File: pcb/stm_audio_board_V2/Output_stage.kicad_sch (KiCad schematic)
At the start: 29 parts, among them U2 OP275

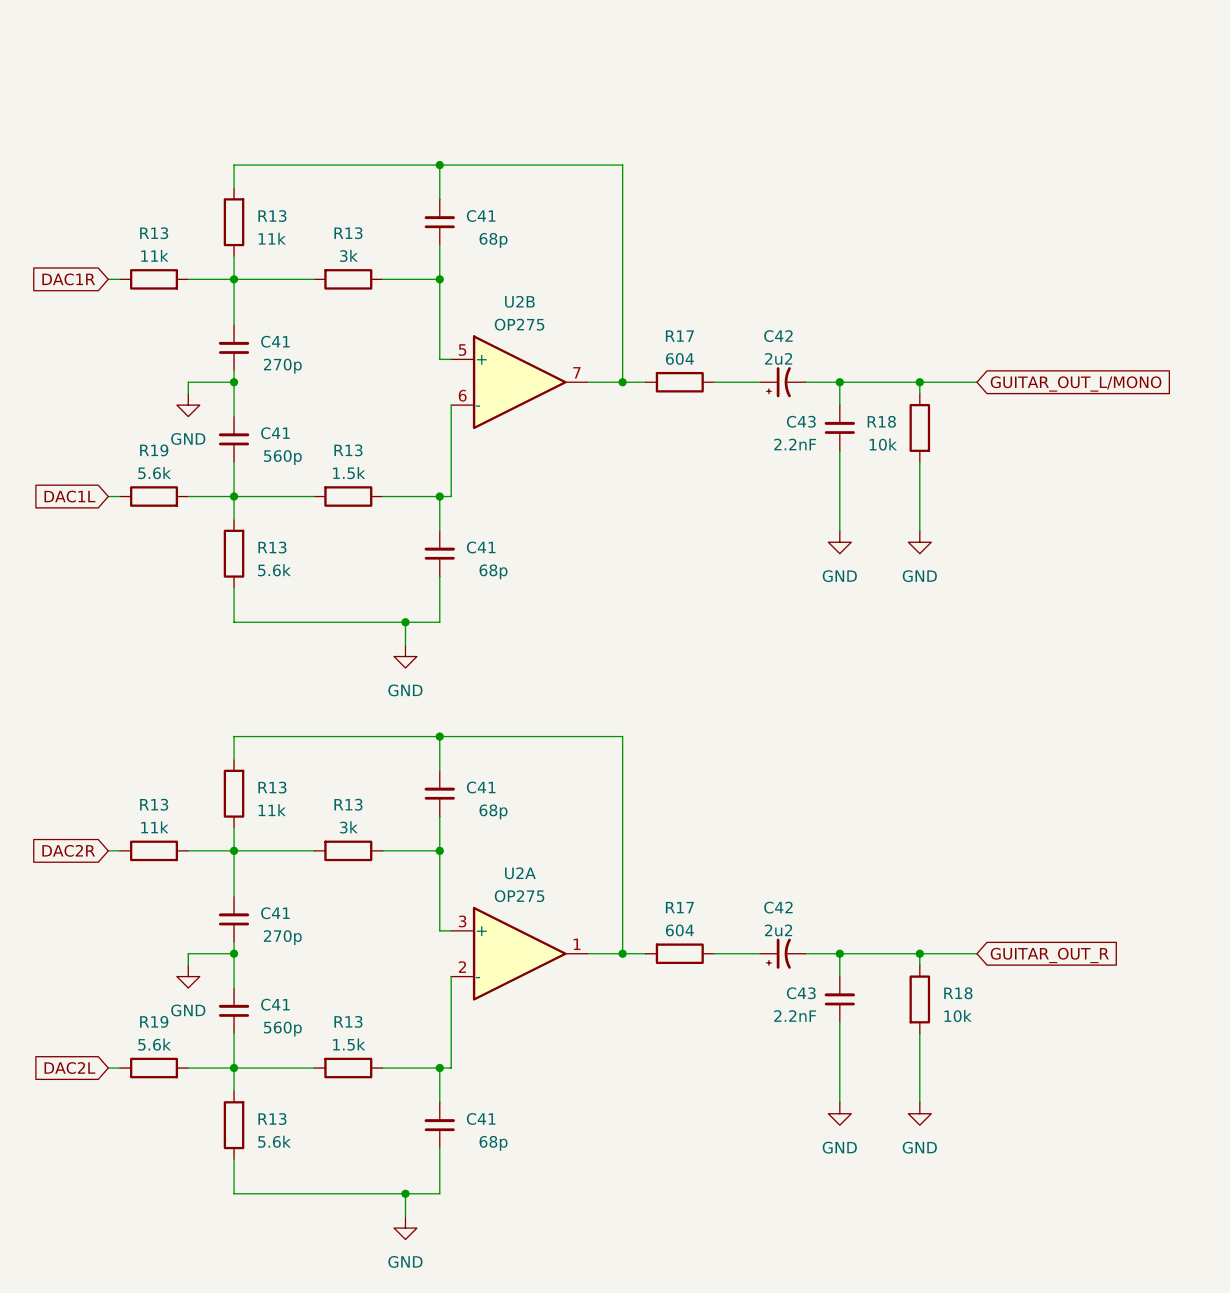
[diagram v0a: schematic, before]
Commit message: some pcb errors are labeled
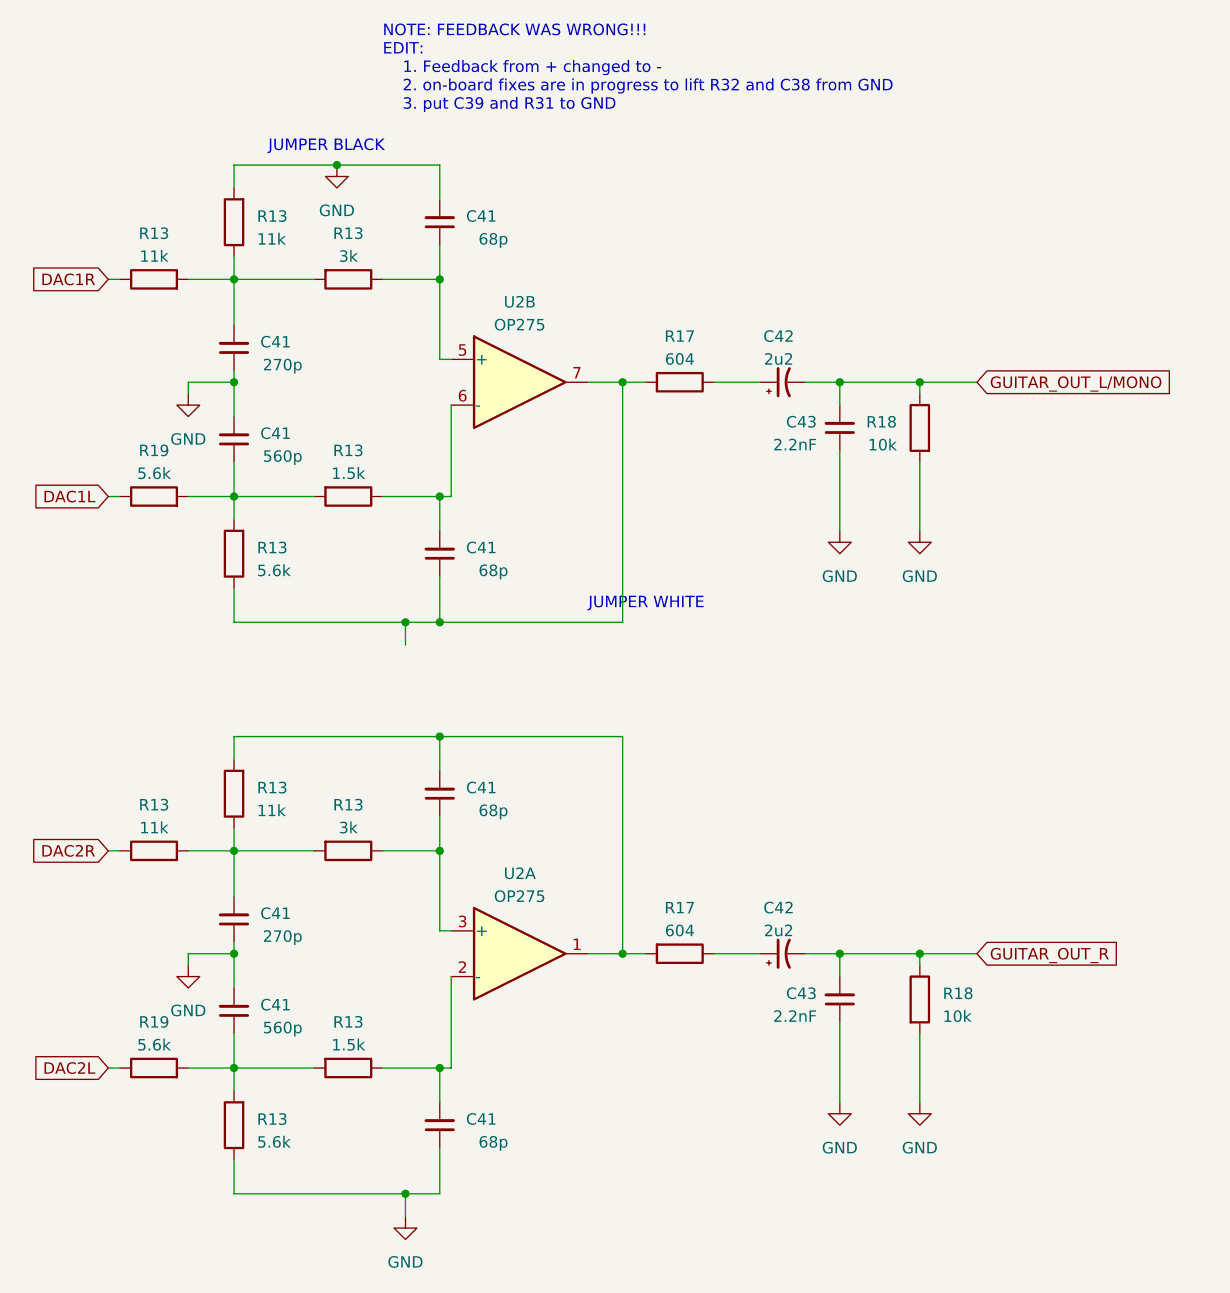
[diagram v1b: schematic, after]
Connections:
- net GND: now also C41.2, R13.2; no longer C41.1, R13.1
- net at R17.2, U2.7: now also C41.1, R13.1; no longer C41.2, R13.2
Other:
- note added: "JUMPER BLACK"
- note added: "JUMPER WHITE"
- note added: "NOTE: FEEDBACK WAS WRONG!!! EDIT: 1. Feedback from + changed to - 2. on-board fixes are in progress to lift R32 and C38 from GND 3. put C39 and R31 to GND"
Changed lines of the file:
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@@
   (junction (at 111.76 160.02) (diameter 0) (color 0 0 0 0)
   )
+  (junction (at 115.57 96.52) (diameter 0) (color 0 0 0 0)
+  )
   (junction (at 111.76 96.52) (diameter 0) (color 0 0 0 0)
   )
   (junction (at 92.71 121.92) (diameter 0) (color 0 0 0 0)
   )
-  (junction (at 115.57 45.72) (diameter 0) (color 0 0 0 0)
-  )
   (junction (at 115.57 58.42) (diameter 0) (color 0 0 0 0)
   )
+  (junction (at 104.14 45.72) (diameter 0) (color 0 0 0 0)
+  )
   (junction (at 160.02 133.35) (diameter 0) (color 0 0 0 0)
   )
@@
     (stroke (width 0) (type default))
   )
-  (wire (pts (xy 92.71 45.72) (xy 115.57 45.72))
+  (wire (pts (xy 92.71 45.72) (xy 104.14 45.72))
     (stroke (width 0) (type default))
   )
@@
     (stroke (width 0) (type default))
   )
-  (wire (pts (xy 115.57 45.72) (xy 135.89 45.72))
-    (stroke (width 0) (type default))
-  )
   (wire (pts (xy 78.74 121.92) (xy 80.01 121.92))
     (stroke (width 0) (type default))
@@
     (stroke (width 0) (type default))
   )
-  (wire (pts (xy 135.89 45.72) (xy 135.89 69.85))
-    (stroke (width 0) (type default))
-  )
   (wire (pts (xy 92.71 142.24) (xy 92.71 146.05))
     (stroke (width 0) (type default))
@@
     (stroke (width 0) (type default))
   )
+  (wire (pts (xy 135.89 96.52) (xy 115.57 96.52))
+    (stroke (width 0) (type default))
+  )
   (wire (pts (xy 78.74 58.42) (xy 80.01 58.42))
     (stroke (width 0) (type default))
@@
     (stroke (width 0) (type default))
   )
+  (wire (pts (xy 104.14 45.72) (xy 115.57 45.72))
+    (stroke (width 0) (type default))
+  )
   (wire (pts (xy 92.71 119.38) (xy 92.71 121.92))
     (stroke (width 0) (type default))
@@
     (stroke (width 0) (type default))
   )
+  (wire (pts (xy 135.89 69.85) (xy 135.89 96.52))
+    (stroke (width 0) (type default))
+  )
   (wire (pts (xy 111.76 160.02) (xy 111.76 162.56))
     (stroke (width 0) (type default))
@@
   (wire (pts (xy 92.71 96.52) (xy 111.76 96.52))
     (stroke (width 0) (type default))
+  )
+  (text "JUMPER BLACK" (at 96.52 44.45 0)
+    (effects (font (size 1.27 1.27)) (justify left bottom))
+  )
+  (text "NOTE: FEEDBACK WAS WRONG!!!\nEDIT: \n	1. Feedback from + changed to -\n	2. on-board fixes are in progress to lift R32 and C38 from GND\n	3. put C39 and R31 to GND\n\n"
+    (at 109.22 41.91 0)
+    (effects (font (size 1.27 1.27)) (justify left bottom))
+  )
+  (text "JUMPER WHITE" (at 132.08 95.25 0)
+    (effects (font (size 1.27 1.27)) (justify left bottom))
   )
   (global_label "GUITAR_OUT_L{slash}MONO" (shape input) (at 175.26 69.85 0) (fields_autoplaced)
@@
     (property "Intersheetrefs" "${INTERSHEET_REFS}" (at 69.968 146.05 0)
       (effects (font (size 1.27 1.27)) (justify right) hide)
+    )
+  )
+  (symbol (lib_id "power:GND") (at 104.14 45.72 0) (unit 1)
+    (in_bom yes) (on_board yes) (dnp no) (fields_autoplaced)
+    (property "Reference" "#PWR02" (at 104.14 52.07 0)
+      (effects (font (size 1.27 1.27)) hide)
+    )
+    (property "Value" "GND" (at 104.14 50.8 0)
+      (effects (font (size 1.27 1.27)))
+    )
+    (property "Footprint" "" (at 104.14 45.72 0)
+      (effects (font (size 1.27 1.27)) hide)
+    )
+    (property "Datasheet" "" (at 104.14 45.72 0)
+      (effects (font (size 1.27 1.27)) hide)
+    )
+    (pin "1")
+    (instances
+      (project "stm_audio_board_V2"
+        (path "/6997cf63-2615-4e49-9471-e7da1b6bae71"
+          (reference "#PWR02") (unit 1)
+        )
+        (path "/6997cf63-2615-4e49-9471-e7da1b6bae71/2eb2ee8f-ab98-4666-97f0-bfacb073bc88"
+          (reference "#PWR01") (unit 1)
+        )
+        (path "/6997cf63-2615-4e49-9471-e7da1b6bae71/83920463-7bb1-4088-aad8-702bcdea14ea"
+          (reference "#PWR015") (unit 1)
+        )
+      )
     )
   )
@@
         )
       )
-    )
-  )
-  (symbol (lib_id "power:GND") (at 111.76 99.06 0) (unit 1)
-    (in_bom yes) (on_board yes) (dnp no) (fields_autoplaced)
-    (property "Reference" "#PWR02" (at 111.76 105.41 0)
-      (effects (font (size 1.27 1.27)) hide)
-    )
-    (property "Value" "GND" (at 111.76 104.14 0)
-      (effects (font (size 1.27 1.27)))
-    )
-    (property "Footprint" "" (at 111.76 99.06 0)
-      (effects (font (size 1.27 1.27)) hide)
-    )
-    (property "Datasheet" "" (at 111.76 99.06 0)
-      (effects (font (size 1.27 1.27)) hide)
-    )
-    (pin "1")
-    (instances
-      (project "stm_audio_board_V2"
-        (path "/6997cf63-2615-4e49-9471-e7da1b6bae71"
-          (reference "#PWR02") (unit 1)
-        )
-        (path "/6997cf63-2615-4e49-9471-e7da1b6bae71/2eb2ee8f-ab98-4666-97f0-bfacb073bc88"
-          (reference "#PWR01") (unit 1)
-        )
-        (path "/6997cf63-2615-4e49-9471-e7da1b6bae71/83920463-7bb1-4088-aad8-702bcdea14ea"
-          (reference "#PWR015") (unit 1)
-        )
-      )
